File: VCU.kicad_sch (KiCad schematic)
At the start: 36 parts, among them J2 2x3_Conn, J3 USB_C_Receptacle_USB2.0_14P, SW1 SW_Push, SW2 SW_Push, U1 ESP32-S3-WROOM-1, U2 LM1117DT-3.3, U3 SN65HVD230, U4 USBLC6-2SC6, U6 MCP6001-OT

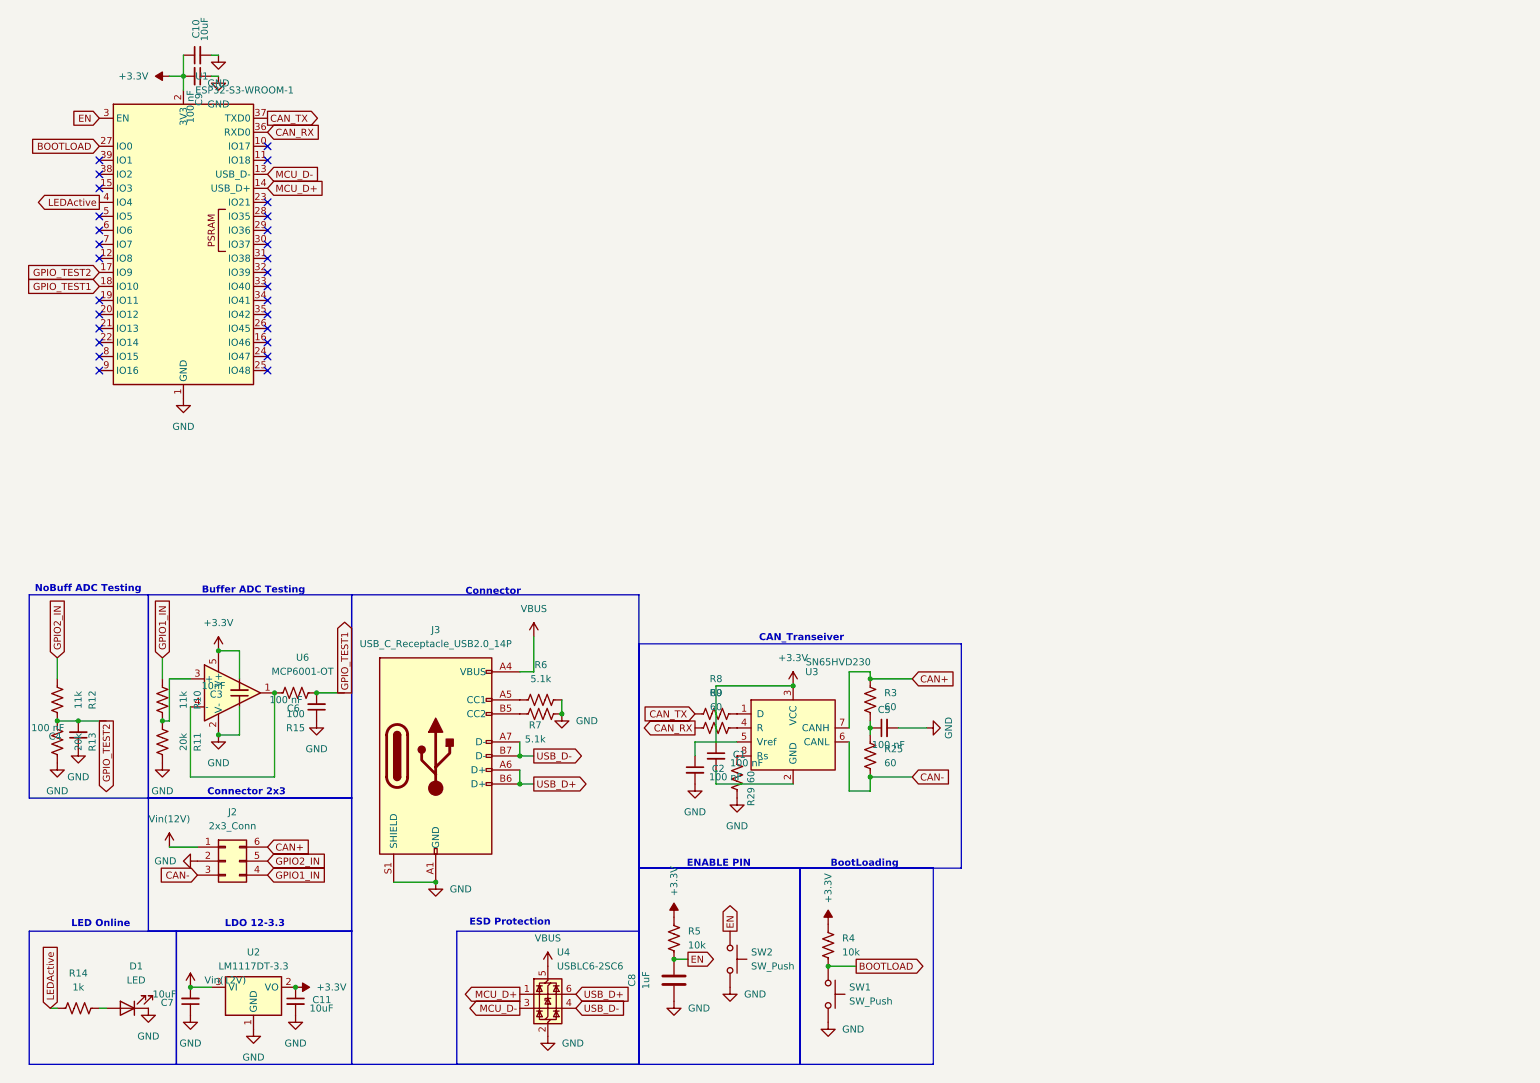
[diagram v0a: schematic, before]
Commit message: ADD CAN-FD to schem
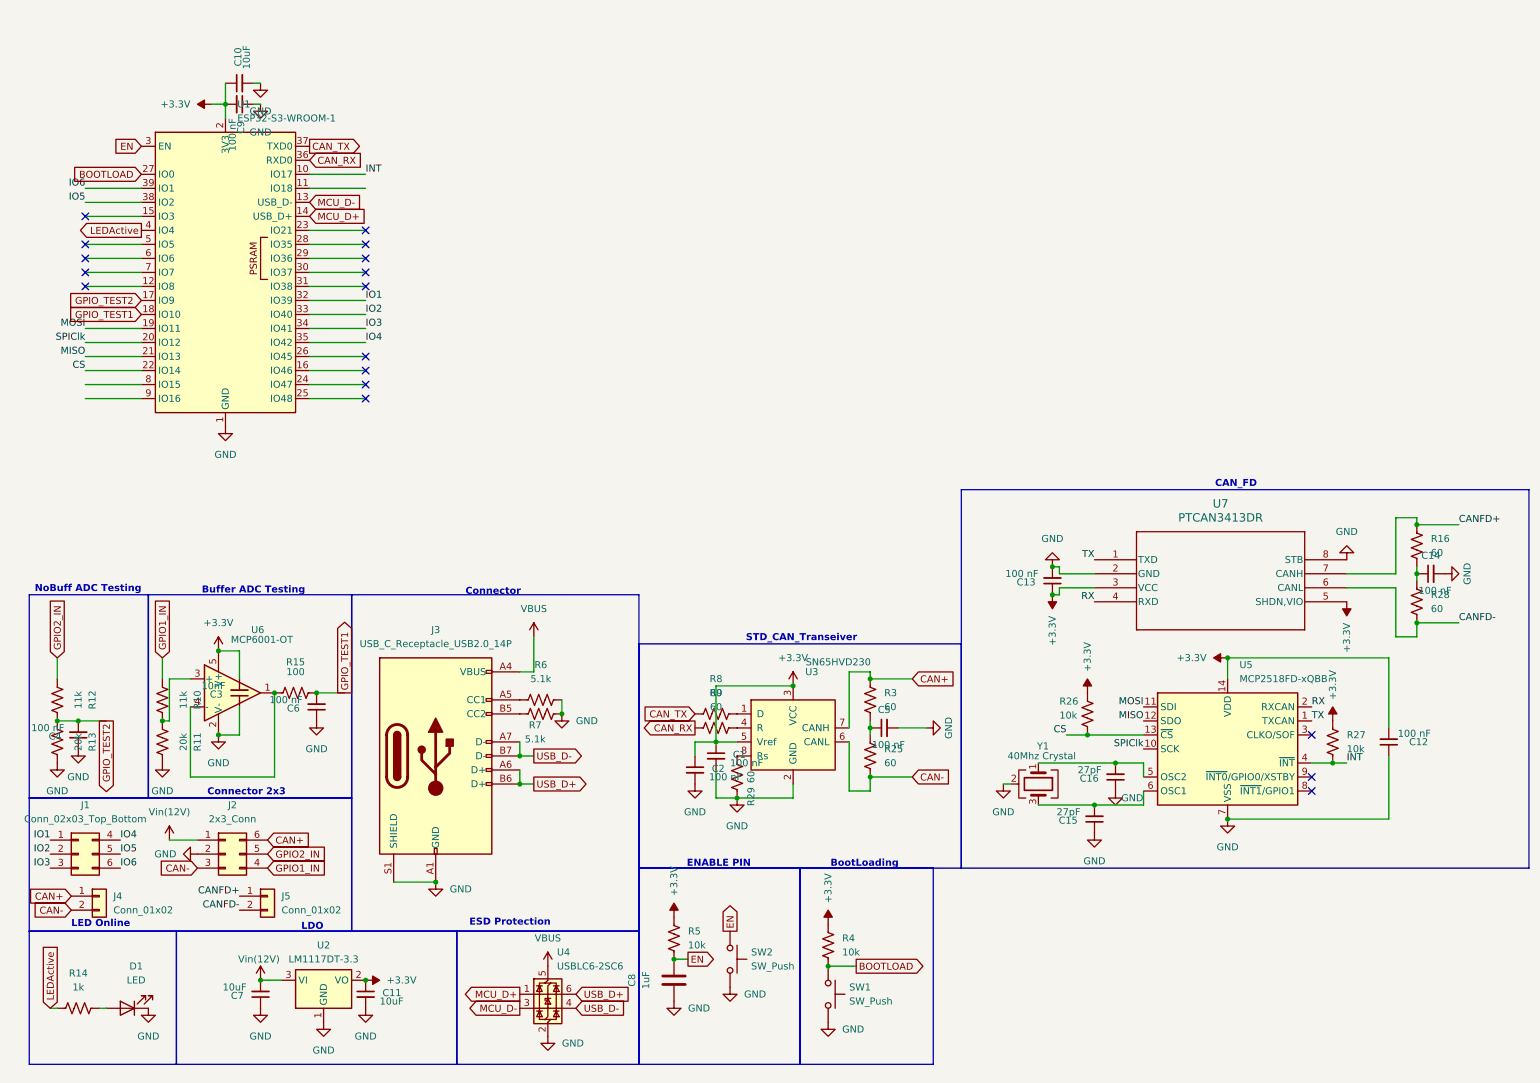
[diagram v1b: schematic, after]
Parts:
- added C12, C13, C14: 100 nF, Capacitor_SMD:C_0805_2012Metric, symbol Device:C_Small
- added C15, C16: 27pF, Capacitor_SMD:C_0805_2012Metric, symbol Device:C_Small
- added J1: Conn_02x03_Top_Bottom, Connector_PinHeader_2.54mm:PinHeader_2x03_P2.54mm_Vertical, symbol Connector_Generic:Conn_02x03_Top_Bottom
- added J4: Conn_01x02, Connector_PinHeader_2.54mm:PinHeader_1x02_P2.54mm_Vertical, symbol Connector_Generic:Conn_01x02
- added J5: Conn_01x02, Connector_Molex:Molex_Mini-Fit_Jr_5566-02A_2x01_P4.20mm_Vertical, symbol Connector_Generic:Conn_01x02
- added R16, R28: 60, Resistor_SMD:R_0805_2012Metric, symbol Device:R_US
- added R26, R27: 10k, Resistor_SMD:R_0805_2012Metric, symbol Device:R_US
- added U5: MCP2518FD-xQBB, Package_DFN_QFN:DFN-14-1EP_3x4.5mm_P0.65mm_EP1.65x4.25mm, symbol Interface_CAN_LIN:MCP2518FD-xQBB
- added U7: PTCAN3413DR, SOIC8_D_TEX, symbol can-fd-trans:PTCAN3413DR
- added Y1: 40Mhz Crystal, Crystal:Crystal_SMD_3225-4Pin_3.2x2.5mm, symbol Device:Crystal_GND24
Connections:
- net +3.3V: now also C2.1, U3.5 (Vref), C12.2, C13.1, R26.1, R27.2, U5.14 (VDD), U7.3 (VCC), U7.5 (SHDN,VIO)
- net CAN+: now also J4.1 (Pin_1)
- net CAN-: now also J4.2 (Pin_2)
- net GND: now also C1.2, U3.2 (GND), C12.1, C13.2, C14.2, C15.1, C16.1, U5.15 (VSS), U5.7 (VSS), U7.2 (GND), U7.8 (STB), Y1.2 (G), Y1.4 (G)
- net GPIO_TEST1: now also R15.2; no longer R15.1
- net at U6.1, U6.4 (-): now also R15.1; no longer R15.2
- net INT: now reaches U1.10 (IO17)
- net INT: now also R27.1, U5.4 (~{INT})
- net MOSI: now reaches U1.19 (IO11)
- net MOSI: now also U5.11 (SDI)
- net SPIClk: now reaches U1.20 (IO12)
- net SPIClk: now also U5.10 (SCK)
- net MISO: now reaches U1.21 (IO13)
- net MISO: now also U5.12 (SDO)
- net CS: now reaches U1.22 (IO14)
- net CS: now also R26.2, U5.13 (~{CS})
- net IO1: now reaches U1.32 (IO39)
- net IO1: now also J1.1 (Pin_1)
- net IO2: now reaches U1.33 (IO40)
- net IO2: now also J1.2 (Pin_2)
- net IO3: now reaches U1.34 (IO41)
- net IO3: now also J1.3 (Pin_3)
- net IO4: now reaches U1.35 (IO42)
- net IO4: now also J1.4 (Pin_4)
- net IO5: now reaches U1.38 (IO2)
- net IO5: now also J1.5 (Pin_5)
- net IO6: now reaches U1.39 (IO1)
- net IO6: now also J1.6 (Pin_6)
- new net: C14.1, R16.2, R28.1
- new net: C16.2, U5.5 (OSC2), Y1.1
- new net: C15.2, U5.6 (OSC1), Y1.3
- new net CANFD+: J5.1 (Pin_1), R16.1, U7.7 (CANH)
- new net CANFD-: J5.2 (Pin_2), R28.2, U7.6 (CANL)
- new net RX: U5.2 (RXCAN), U7.4 (RXD)
- new net TX: U5.1 (TXCAN), U7.1 (TXD)
- no-connect marks 28 -> 17
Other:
- note added: "CAN_FD"
- note added: "LDO"
- note added: "STD_CAN_Transeiver"
- note removed: "CAN_Transeiver"
- note removed: "LDO 12-3.3"

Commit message: Do Layout
Yuh
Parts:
- removed J4: Conn_01x02, Connector_PinHeader_2.54mm:PinHeader_1x02_P2.54mm_Vertical, symbol Connector_Generic:Conn_01x02
- U4: footprint SK's_Components:ESD_SOT-23-6 -> Package_TO_SOT_SMD:SOT-23-6
- U7: footprint SOIC8_D_TEX -> KiCADv6:SOIC8_D_TEX
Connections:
- net CAN+: now also J5.1 (Pin_1); no longer J2.6 (Pin_6)
- net CAN-: now also J5.2 (Pin_2); no longer J2.3 (Pin_3)
- net CANFD+: now also J2.6 (Pin_6); no longer J5.1 (Pin_1)
- net CANFD-: now also J2.3 (Pin_3); no longer J5.2 (Pin_2)
- net GND: now also J3.SH (SHIELD); no longer J3.S1 (SHIELD)
- net Vin(12V) renamed Vin(5V)
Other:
- moved on the sheet: J5
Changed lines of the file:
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@@
 		)
 	)
-	(label "CANFD-"
-		(at 50.8 170.18 180)
+	(label "INT"
+		(at 251.46 143.51 0)
 		(effects
 			(font
 				(size 1.27 1.27)
 			)
-			(justify right bottom)
+			(justify left bottom)
 		)
 	)
-	(label "INT"
-		(at 251.46 143.51 0)
+	(label "CANFD+"
+		(at 55.88 157.48 0)
 		(effects
 			(font
@@
 		)
 	)
-	(label "CANFD+"
-		(at 50.8 167.64 180)
+	(label "CANFD-"
+		(at 43.18 162.56 180)
 		(effects
 			(font
@@
 		)
 	)
-	(global_label "CAN+"
-		(shape input)
-		(at 55.88 157.48 0)
-		(fields_autoplaced yes)
-		(effects
-			(font
-				(size 1.27 1.27)
-			)
-			(justify left)
-		)
-		(property "Intersheetrefs" "${INTERSHEET_REFS}"
-			(at 64.1267 157.48 0)
-			(hide yes)
-			(show_name no)
-			(do_not_autoplace no)
-			(effects
-				(font
-					(size 1.27 1.27)
-				)
-				(justify left)
-			)
-		)
-	)
-	(global_label "CAN+"
-		(shape input)
-		(at 20.32 167.64 180)
-		(fields_autoplaced yes)
-		(effects
-			(font
-				(size 1.27 1.27)
-			)
-			(justify right)
-		)
-		(property "Intersheetrefs" "${INTERSHEET_REFS}"
-			(at 12.0733 167.64 0)
-			(hide yes)
-			(show_name no)
-			(do_not_autoplace no)
-			(effects
-				(font
-					(size 1.27 1.27)
-				)
-				(justify right)
-			)
-		)
-	)
 	(global_label "CAN_RX"
 		(shape output)
@@
 		)
 	)
-	(global_label "CAN-"
-		(shape input)
-		(at 43.18 162.56 180)
-		(fields_autoplaced yes)
-		(effects
-			(font
-				(size 1.27 1.27)
-			)
-			(justify right)
-		)
-		(property "Intersheetrefs" "${INTERSHEET_REFS}"
-			(at 34.9333 162.56 0)
-			(hide yes)
-			(show_name no)
-			(do_not_autoplace no)
-			(effects
-				(font
-					(size 1.27 1.27)
-				)
-				(justify right)
-			)
-		)
-	)
 	(global_label "EN"
 		(shape input)
@@
 		)
 	)
+	(global_label "CAN-"
+		(shape input)
+		(at 22.86 168.91 180)
+		(fields_autoplaced yes)
+		(effects
+			(font
+				(size 1.27 1.27)
+			)
+			(justify right)
+		)
+		(property "Intersheetrefs" "${INTERSHEET_REFS}"
+			(at 14.6133 168.91 0)
+			(hide yes)
+			(show_name no)
+			(do_not_autoplace no)
+			(effects
+				(font
+					(size 1.27 1.27)
+				)
+				(justify right)
+			)
+		)
+	)
 	(global_label "LEDActive"
 		(shape output)
@@
 		)
 	)
-	(global_label "CAN-"
-		(shape input)
-		(at 20.32 170.18 180)
+	(global_label "EN"
+		(shape output)
+		(at 139.7 173.99 90)
 		(fields_autoplaced yes)
 		(effects
@@
 				(size 1.27 1.27)
 			)
-			(justify right)
+			(justify left)
 		)
 		(property "Intersheetrefs" "${INTERSHEET_REFS}"
-			(at 12.0733 170.18 0)
+			(at 139.7 168.5253 90)
 			(hide yes)
 			(show_name no)
@@
 					(size 1.27 1.27)
 				)
-				(justify right)
+				(justify left)
 			)
 		)
 	)
-	(global_label "EN"
-		(shape output)
-		(at 139.7 173.99 90)
+	(global_label "CAN+"
+		(shape input)
+		(at 22.86 166.37 180)
 		(fields_autoplaced yes)
 		(effects
@@
 				(size 1.27 1.27)
 			)
-			(justify left)
+			(justify right)
 		)
 		(property "Intersheetrefs" "${INTERSHEET_REFS}"
-			(at 139.7 168.5253 90)
+			(at 14.6133 166.37 0)
 			(hide yes)
 			(show_name no)
@@
 					(size 1.27 1.27)
 				)
-				(justify left)
+				(justify right)
 			)
 		)
@@
 		(in_pos_files yes)
 		(dnp no)
-		(fields_autoplaced yes)
 		(property "Reference" "#PWR05"
 			(at 38.1 161.29 0)
@@
 			)
 		)
-		(property "Value" "Vin(12V)"
-			(at 38.1 152.4 0)
+		(property "Value" "Vin(5V)"
+			(at 37.592 153.924 0)
 			(show_name no)
 			(do_not_autoplace no)
@@
 					(size 1.27 1.27)
 				)
+				(justify left)
 			)
 		)
@@
 			)
 		)
-		(property "Footprint" "SK's_Components:ESD_SOT-23-6"
+		(property "Footprint" "Package_TO_SOT_SMD:SOT-23-6"
 			(at 107.95 191.77 0)
 			(hide yes)
@@
 	)
 	(symbol
-		(lib_id "Connector_Generic:Conn_01x02")
-		(at 25.4 167.64 0)
-		(unit 1)
-		(body_style 1)
-		(exclude_from_sim no)
-		(in_bom yes)
-		(on_board yes)
-		(in_pos_files yes)
-		(dnp no)
-		(fields_autoplaced yes)
-		(property "Reference" "J4"
-			(at 27.94 167.6399 0)
-			(show_name no)
-			(do_not_autoplace no)
-			(effects
-				(font
-					(size 1.27 1.27)
-				)
-				(justify left)
-			)
-		)
-		(property "Value" "Conn_01x02"
-			(at 27.94 170.1799 0)
-			(show_name no)
-			(do_not_autoplace no)
-			(effects
-				(font
-					(size 1.27 1.27)
-				)
-				(justify left)
-			)
-		)
-		(property "Footprint" "Connector_PinHeader_2.54mm:PinHeader_1x02_P2.54mm_Vertical"
-			(at 25.4 167.64 0)
-			(hide yes)
-			(show_name no)
-			(do_not_autoplace no)
-			(effects
-				(font
-					(size 1.27 1.27)
-				)
-			)
-		)
-		(property "Datasheet" ""
-			(at 25.4 167.64 0)
-			(hide yes)
-			(show_name no)
-			(do_not_autoplace no)
-			(effects
-				(font
-					(size 1.27 1.27)
-				)
-			)
-		)
-		(property "Description" "Generic connector, single row, 01x02, script generated (kicad-library-utils/schlib/autogen/connector/)"
-			(at 25.4 167.64 0)
-			(hide yes)
-			(show_name no)
-			(do_not_autoplace no)
-			(effects
-				(font
-					(size 1.27 1.27)
-				)
-			)
-		)
-		(pin "1"
-		)
-		(pin "2"
-		)
-		(instances
-			(project "VCU"
-				(path "/be7bcd62-a01d-4d10-b317-838a6e59e497"
-					(reference "J4")
-					(unit 1)
-				)
-			)
-		)
-	)
-	(symbol
 		(lib_id "power:GND")
 		(at 205.74 156.21 0)
@@
 	)
 	(symbol
-		(lib_name "USB_C_Receptacle_USB2.0_14P_1")
 		(lib_id "Connector:USB_C_Receptacle_USB2.0_14P")
 		(at 86.36 142.24 0)
@@
 		(pin "B9"
 		)
-		(pin "S1"
+		(pin "SH"
 		)
 		(instances
@@
 		(dnp no)
 		(property "Reference" "C8"
-			(at 121.92 182.88 90)
+			(at 124.968 183.134 90)
 			(show_name no)
 			(do_not_autoplace no)
@@
 		)
 		(property "Value" "1uF"
-			(at 124.46 182.88 90)
+			(at 126.492 182.88 90)
 			(show_name no)
 			(do_not_autoplace no)
@@
 			)
 		)
-		(property "Value" "Vin(12V)"
+		(property "Value" "Vin(5V)"
 			(at 50.546 179.07 0)
 			(show_name no)
@@
 	(symbol
 		(lib_id "Connector_Generic:Conn_01x02")
-		(at 55.88 167.64 0)
+		(at 27.94 166.37 0)
 		(unit 1)
 		(body_style 1)
@@
 		(fields_autoplaced yes)
 		(property "Reference" "J5"
-			(at 58.42 167.6399 0)
+			(at 30.48 166.3699 0)
 			(show_name no)
 			(do_not_autoplace no)
@@
 		)
 		(property "Value" "Conn_01x02"
-			(at 58.42 170.1799 0)
+			(at 30.48 168.9099 0)
 			(show_name no)
 			(do_not_autoplace no)
@@
 		)
 		(property "Footprint" "Connector_Molex:Molex_Mini-Fit_Jr_5566-02A_2x01_P4.20mm_Vertical"
-			(at 55.88 167.64 0)
+			(at 27.94 166.37 0)
 			(hide yes)
 			(show_name no)
@@
 		)
 		(property "Datasheet" ""
-			(at 55.88 167.64 0)
+			(at 27.94 166.37 0)
 			(hide yes)
 			(show_name no)
@@
 		)
 		(property "Description" "Generic connector, single row, 01x02, script generated (kicad-library-utils/schlib/autogen/connector/)"
-			(at 55.88 167.64 0)
+			(at 27.94 166.37 0)
 			(hide yes)
 			(show_name no)
@@
 		)
 		(property "Value" "GND"
-			(at 39.37 160.0199 90)
+			(at 41.91 156.21 90)
 			(show_name no)
 			(do_not_autoplace no)
@@
 					(size 1.27 1.27)
 				)
-				(justify right)
 			)
 		)
@@
 			)
 		)
-		(property "Footprint" "SOIC8_D_TEX"
+		(property "Footprint" "KiCADv6:SOIC8_D_TEX"
 			(at 205.74 106.68 0)
 			(hide yes)

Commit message: ERC, DRC
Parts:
- removed SW1: SW_Push, SK's_Components:Button_MJTP1250, symbol Switch:SW_Push
- added SW3: SW_Push, SK's_Components:Button_MJTP1250, symbol Switch:SW_Push
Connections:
- net +3.3V: no longer C2.1, U3.5 (Vref)
- net BOOTLOAD: now also SW3.1
- net GND: now also SW3.2
- net GPIO_TEST1: now also R15.1; no longer R15.2
- net at U6.1, U6.4 (-): now also R15.2; no longer R15.1
- new net: C2.1, U3.5 (Vref)
- no-connect marks 17 -> 20
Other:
- moved on the sheet: R15
